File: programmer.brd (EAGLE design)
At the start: 35.3 x 22.1 mm, 20 parts, among them IC1 74ABT125DB, U1 ATMEGA8U2, X1 16MHz

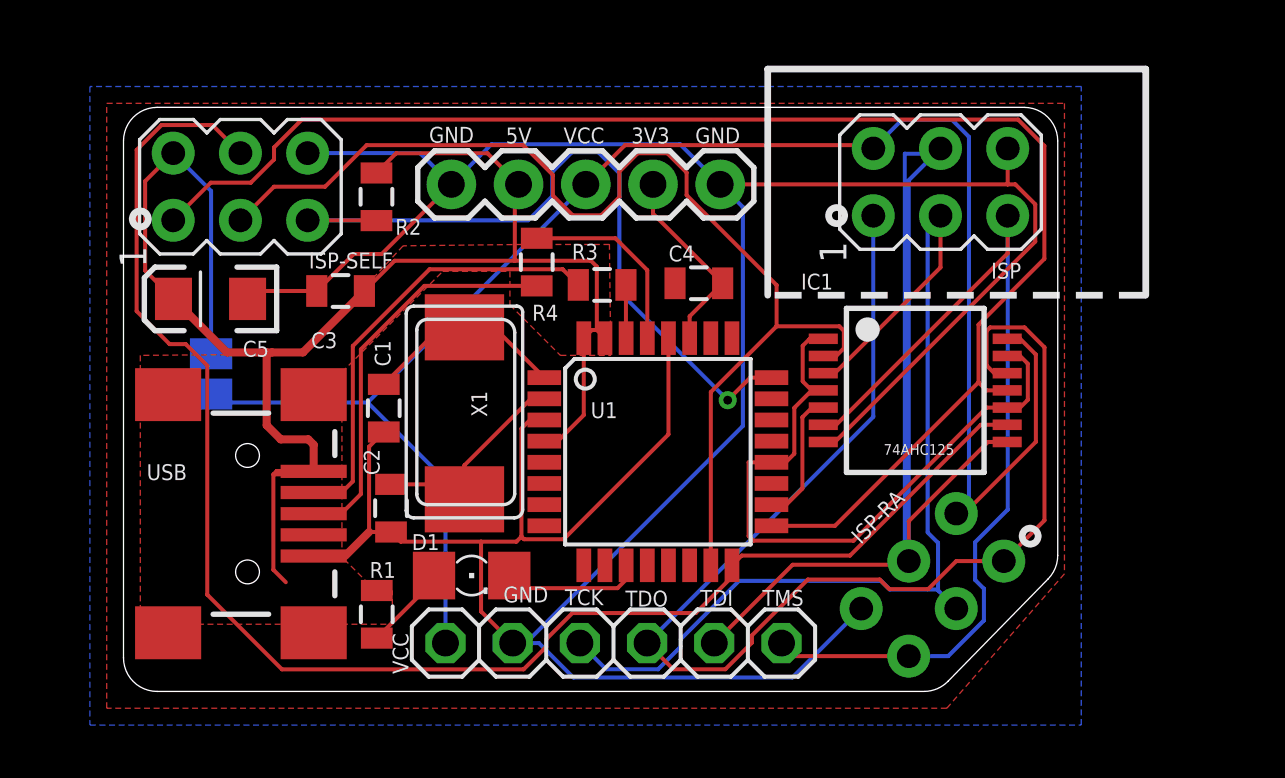
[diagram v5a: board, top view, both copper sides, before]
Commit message: Improved power and GND polygons, moved sowbug.com to a place where it won't get drilled
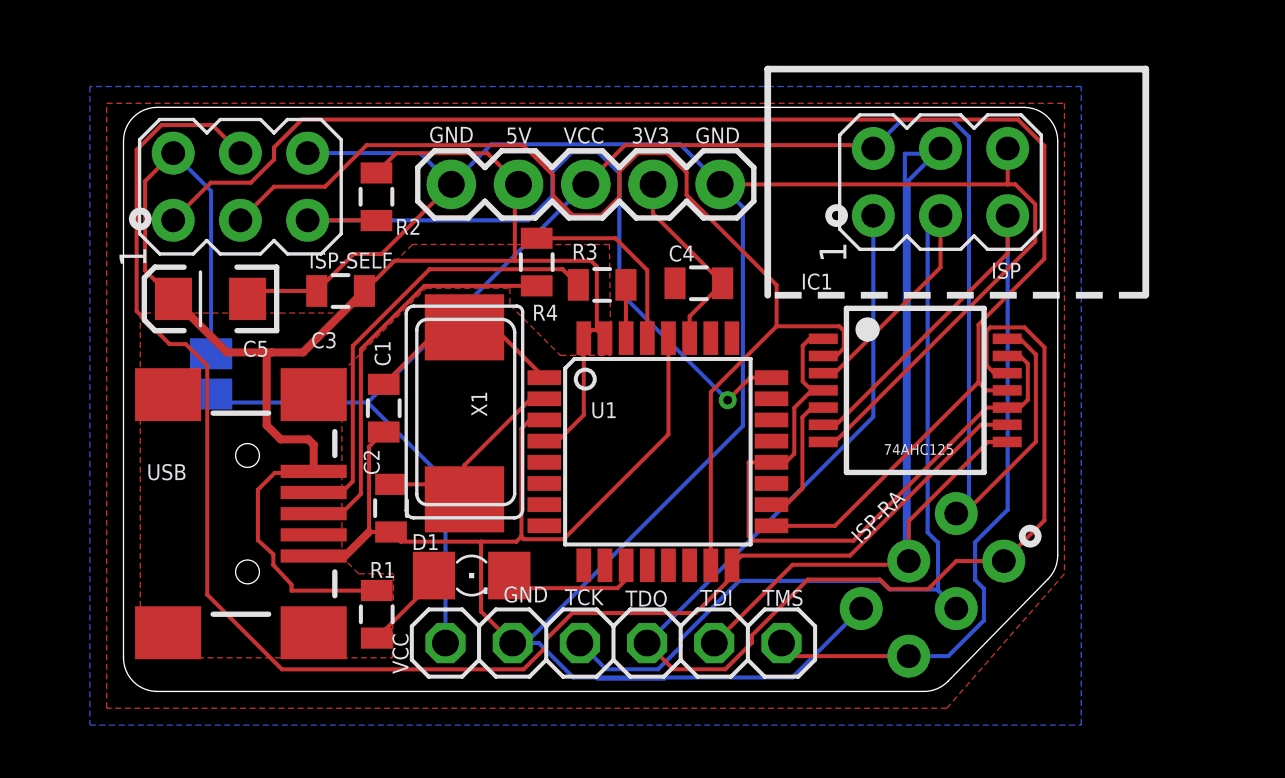
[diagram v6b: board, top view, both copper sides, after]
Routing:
- net 5V: track 64.1 -> 67.7 mm
- net N$1: track 0.00 -> 2.54 mm
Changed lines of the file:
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@@
 <layer number="19" name="Unrouted" color="6" fill="1" visible="yes" active="yes"/>
 <layer number="20" name="Dimension" color="15" fill="1" visible="yes" active="yes"/>
-<layer number="21" name="tPlace" color="7" fill="1" visible="yes" active="yes"/>
+<layer number="21" name="tPlace" color="7" fill="1" visible="no" active="yes"/>
 <layer number="22" name="bPlace" color="7" fill="1" visible="yes" active="yes"/>
-<layer number="23" name="tOrigins" color="15" fill="1" visible="yes" active="yes"/>
+<layer number="23" name="tOrigins" color="15" fill="1" visible="no" active="yes"/>
 <layer number="24" name="bOrigins" color="15" fill="1" visible="yes" active="yes"/>
-<layer number="25" name="tNames" color="7" fill="1" visible="yes" active="yes"/>
+<layer number="25" name="tNames" color="7" fill="1" visible="no" active="yes"/>
 <layer number="26" name="bNames" color="7" fill="1" visible="yes" active="yes"/>
 <layer number="27" name="tValues" color="7" fill="1" visible="yes" active="yes"/>
@@
 <layer number="37" name="tTest" color="7" fill="1" visible="no" active="yes"/>
 <layer number="38" name="bTest" color="7" fill="1" visible="no" active="yes"/>
-<layer number="39" name="tKeepout" color="4" fill="11" visible="yes" active="yes"/>
-<layer number="40" name="bKeepout" color="1" fill="11" visible="yes" active="yes"/>
-<layer number="41" name="tRestrict" color="4" fill="10" visible="yes" active="yes"/>
-<layer number="42" name="bRestrict" color="1" fill="10" visible="yes" active="yes"/>
-<layer number="43" name="vRestrict" color="2" fill="10" visible="yes" active="yes"/>
+<layer number="39" name="tKeepout" color="4" fill="11" visible="no" active="yes"/>
+<layer number="40" name="bKeepout" color="1" fill="11" visible="no" active="yes"/>
+<layer number="41" name="tRestrict" color="4" fill="10" visible="no" active="yes"/>
+<layer number="42" name="bRestrict" color="1" fill="10" visible="no" active="yes"/>
+<layer number="43" name="vRestrict" color="2" fill="10" visible="no" active="yes"/>
 <layer number="44" name="Drills" color="7" fill="1" visible="no" active="yes"/>
 <layer number="45" name="Holes" color="7" fill="1" visible="no" active="yes"/>
 <layer number="46" name="Milling" color="3" fill="1" visible="no" active="yes"/>
 <layer number="47" name="Measures" color="7" fill="1" visible="no" active="yes"/>
-<layer number="48" name="Document" color="7" fill="1" visible="yes" active="yes"/>
-<layer number="49" name="Reference" color="7" fill="1" visible="yes" active="yes"/>
+<layer number="48" name="Document" color="7" fill="1" visible="no" active="yes"/>
+<layer number="49" name="Reference" color="7" fill="1" visible="no" active="yes"/>
 <layer number="50" name="dxf" color="7" fill="1" visible="no" active="no"/>
-<layer number="51" name="tDocu" color="7" fill="1" visible="yes" active="yes"/>
+<layer number="51" name="tDocu" color="7" fill="1" visible="no" active="yes"/>
 <layer number="52" name="bDocu" color="7" fill="1" visible="yes" active="yes"/>
 <layer number="53" name="tGND_GNDA" color="7" fill="9" visible="no" active="no"/>
@@
 <layer number="109" name="fp9" color="7" fill="1" visible="no" active="yes"/>
 <layer number="110" name="fp0" color="7" fill="1" visible="no" active="yes"/>
-<layer number="111" name="LPC17xx" color="7" fill="1" visible="yes" active="yes"/>
-<layer number="112" name="tSilk" color="7" fill="1" visible="yes" active="yes"/>
+<layer number="111" name="LPC17xx" color="7" fill="1" visible="no" active="yes"/>
+<layer number="112" name="tSilk" color="7" fill="1" visible="no" active="yes"/>
 <layer number="116" name="Patch_BOT" color="9" fill="4" visible="no" active="yes"/>
 <layer number="121" name="_tsilk" color="7" fill="1" visible="no" active="yes"/>
@@
 <layer number="124" name="bTestmark" color="7" fill="1" visible="no" active="yes"/>
 <layer number="125" name="_tNames" color="7" fill="1" visible="no" active="yes"/>
-<layer number="126" name="_bNames" color="7" fill="1" visible="yes" active="yes"/>
-<layer number="127" name="_tValues" color="7" fill="1" visible="yes" active="yes"/>
-<layer number="128" name="_bValues" color="7" fill="1" visible="yes" active="yes"/>
+<layer number="126" name="_bNames" color="7" fill="1" visible="no" active="yes"/>
+<layer number="127" name="_tValues" color="7" fill="1" visible="no" active="yes"/>
+<layer number="128" name="_bValues" color="7" fill="1" visible="no" active="yes"/>
 <layer number="131" name="tAdjust" color="7" fill="1" visible="no" active="yes"/>
 <layer number="132" name="bAdjust" color="7" fill="1" visible="no" active="yes"/>
 <layer number="144" name="Drill_legend" color="7" fill="1" visible="no" active="yes"/>
 <layer number="151" name="HeatSink" color="7" fill="1" visible="no" active="yes"/>
-<layer number="152" name="_bDocu" color="7" fill="1" visible="yes" active="yes"/>
-<layer number="199" name="Contour" color="7" fill="1" visible="yes" active="yes"/>
+<layer number="152" name="_bDocu" color="7" fill="1" visible="no" active="yes"/>
+<layer number="199" name="Contour" color="7" fill="1" visible="no" active="yes"/>
 <layer number="200" name="200bmp" color="1" fill="10" visible="no" active="yes"/>
 <layer number="201" name="201bmp" color="2" fill="10" visible="no" active="yes"/>
@@
 <layer number="223" name="223bmp" color="24" fill="1" visible="no" active="no"/>
 <layer number="224" name="224bmp" color="25" fill="1" visible="no" active="no"/>
-<layer number="248" name="Housing" color="7" fill="1" visible="yes" active="yes"/>
-<layer number="249" name="Edge" color="7" fill="1" visible="yes" active="yes"/>
+<layer number="248" name="Housing" color="7" fill="1" visible="no" active="yes"/>
+<layer number="249" name="Edge" color="7" fill="1" visible="no" active="yes"/>
 <layer number="250" name="Descript" color="3" fill="1" visible="no" active="no"/>
 <layer number="251" name="SMDround" color="12" fill="11" visible="no" active="no"/>
@@
 <wire x1="34.036" y1="22.0726" x2="1.27" y2="22.0726" width="0" layer="20"/>
 <wire x1="1.27" y1="22.0726" x2="0" y2="20.8026" width="0" layer="20" curve="90"/>
-<text x="20.2692" y="16.0274" size="1.778" layer="22" font="vector" ratio="18" rot="MR0" align="bottom-center">sowbug.com</text>
+<text x="19.6342" y="15.3924" size="1.778" layer="22" font="vector" ratio="18" rot="MR0" align="bottom-center">sowbug.com</text>
 <text x="14.7574" y="8.9408" size="1.778" layer="22" font="vector" ratio="18" rot="MR0" align="bottom-right">MISO 1</text>
 <text x="13.4874" y="8.9408" size="1.778" layer="22" font="vector" ratio="18" rot="MR0">2 VCC</text>
@@
 <wire x1="5.3975" y1="12.7" x2="5.4102" y2="12.7" width="0.1524" layer="1"/>
 <wire x1="5.3975" y1="12.7" x2="5.3975" y2="12.8109" width="0.1524" layer="1"/>
-<wire x1="6.1341" y1="4.1275" x2="5.6642" y2="4.5974" width="0.1524" layer="1"/>
 <wire x1="6.8201" y1="8.3312" x2="7.1868" y2="8.3169" width="0.1524" layer="1"/>
-<wire x1="5.6642" y1="4.5974" x2="5.6642" y2="8.2042" width="0.1524" layer="1"/>
-<wire x1="6.8201" y1="8.3312" x2="5.7912" y2="8.3312" width="0.1524" layer="1"/>
-<wire x1="5.7912" y1="8.3312" x2="5.715" y2="8.255" width="0.1524" layer="1"/>
-<wire x1="5.6642" y1="8.2042" x2="7.0741" y2="8.2042" width="0.1524" layer="1"/>
 <wire x1="7.0741" y1="8.2042" x2="7.1868" y2="8.3169" width="0.1524" layer="1"/>
 <polygon width="0.1524" layer="1">
-<vertex x="0.635" y="12.7"/>
-<vertex x="0.635" y="2.54"/>
-<vertex x="10.16" y="2.54"/>
-<vertex x="10.16" y="3.81"/>
-<vertex x="9.525" y="3.81"/>
+<vertex x="0.635" y="14.3002"/>
+<vertex x="0.635" y="1.27"/>
+<vertex x="10.16" y="1.27"/>
+<vertex x="10.2108" y="4.445"/>
+<vertex x="8.89" y="4.445"/>
 <vertex x="8.255" y="5.08"/>
 <vertex x="8.255" y="12.065"/>
-<vertex x="12.065" y="15.875"/>
-<vertex x="14.605" y="15.875"/>
+<vertex x="11.43" y="15.24"/>
+<vertex x="14.605" y="15.24"/>
 <vertex x="14.605" y="14.605"/>
 <vertex x="16.51" y="12.7"/>
 <vertex x="18.415" y="12.7"/>
 <vertex x="18.3642" y="16.891"/>
-<vertex x="15.0622" y="16.891"/>
-<vertex x="10.5664" y="16.8402"/>
-<vertex x="6.7818" y="12.7508"/>
+<vertex x="10.922" y="16.891"/>
+<vertex x="8.3058" y="14.3002"/>
 </polygon>
+<wire x1="9.525" y1="4.1275" x2="9.2075" y2="3.81" width="0.1524" layer="1"/>
+<wire x1="7.1868" y1="8.3169" x2="7.1249" y2="8.255" width="0.1524" layer="1"/>
+<wire x1="7.1249" y1="8.255" x2="5.715" y2="8.255" width="0.1524" layer="1"/>
+<wire x1="5.715" y1="8.255" x2="5.08" y2="7.62" width="0.1524" layer="1"/>
+<wire x1="5.08" y1="7.62" x2="5.08" y2="5.715" width="0.1524" layer="1"/>
+<wire x1="5.08" y1="5.715" x2="5.6642" y2="5.1816" width="0.1524" layer="1"/>
+<wire x1="5.6642" y1="5.1816" x2="5.6642" y2="4.7752" width="0.1524" layer="1"/>
+<wire x1="5.6642" y1="4.7752" x2="6.35" y2="4.0386" width="0.1524" layer="1"/>
+<wire x1="6.35" y1="4.0386" x2="6.35" y2="3.81" width="0.1524" layer="1"/>
+<wire x1="6.35" y1="3.81" x2="9.5676" y2="3.81" width="0.1524" layer="1"/>
+<wire x1="9.5676" y1="3.81" x2="9.5714" y2="3.8138" width="0.1524" layer="1"/>
 </signal>
 <signal name="RST">
@@
 <wire x1="9.5485" y1="17.8043" x2="9.5594" y2="17.7934" width="0.1524" layer="1"/>
 </signal>
+<signal name="N$1">
+<wire x1="17.907" y1="0.4826" x2="20.447" y2="0.4826" width="0.1524" layer="16"/>
+</signal>
 </signals>
+<errors>
+</errors>
 </board>
 </drawing>

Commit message: Beefed up GND on bottom layer; cleaned up messy thermal/routing interaction near uC power
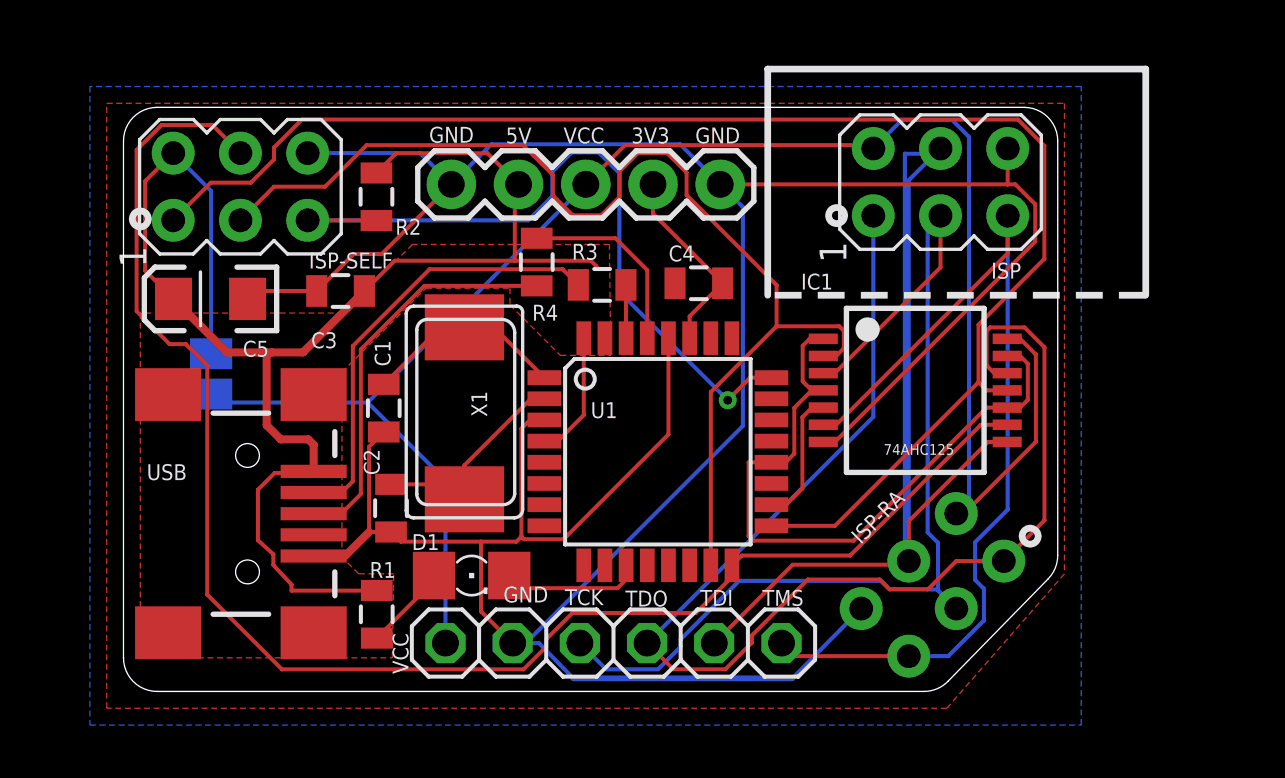
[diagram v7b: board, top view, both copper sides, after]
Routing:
- net 5V: track 67.7 -> 64.3 mm
- net N$1: track 2.54 -> 0.00 mm
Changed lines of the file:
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@@
 <wire x1="13.9079" y1="20.6801" x2="21.0325" y2="20.6801" width="0.1524" layer="16"/>
 <wire x1="21.0325" y1="20.6801" x2="22.5502" y2="19.1624" width="0.1524" layer="16"/>
-<wire x1="15.6981" y1="1.8281" x2="16.9995" y2="0.5267" width="0.1524" layer="16"/>
-<wire x1="16.9995" y1="0.5267" x2="25.2758" y2="0.5267" width="0.1524" layer="16"/>
-<wire x1="25.2758" y1="0.5267" x2="27.8798" y2="3.1307" width="0.1524" layer="16"/>
+<wire x1="15.6981" y1="1.8281" x2="16.9995" y2="0.49368125" width="0.1524" layer="16"/>
+<wire x1="16.9995" y1="0.49368125" x2="25.2758" y2="0.49368125" width="0.2159" layer="16"/>
+<wire x1="25.2758" y1="0.49368125" x2="27.8798" y2="3.1307" width="0.1524" layer="16"/>
 <wire x1="26.4459" y1="9.4269" x2="26.8839" y2="9.4269" width="0.1524" layer="1"/>
 <wire x1="26.8839" y1="9.4269" x2="34.457" y2="17" width="0.1524" layer="1"/>
@@
 <wire x1="17.3949" y1="10.4436" x2="16.4103" y2="9.459" width="0.1524" layer="1"/>
 <wire x1="16.4103" y1="9.459" x2="15.9023" y2="9.459" width="0.1524" layer="1"/>
-<wire x1="17.8875" y1="13.659" x2="17.7023" y2="13.659" width="0.1524" layer="1"/>
-<wire x1="17.7023" y1="13.659" x2="17.3949" y2="13.3516" width="0.1524" layer="1"/>
-<wire x1="17.8875" y1="13.659" x2="17.8875" y2="16.0546" width="0.1524" layer="1"/>
 <wire x1="17.8875" y1="16.0546" x2="17.6656" y2="16.2765" width="0.1524" layer="1"/>
 <wire x1="17.6656" y1="16.2765" x2="14.7881" y2="16.2765" width="0.1524" layer="1"/>
-<wire x1="18.1949" y1="13.3516" x2="17.8875" y2="13.659" width="0.1524" layer="1"/>
 <wire x1="14.9302" y1="19.1624" x2="14.7881" y2="19.0203" width="0.1524" layer="1"/>
 <wire x1="14.7881" y1="19.0203" x2="14.7881" y2="16.2765" width="0.1524" layer="1"/>
@@
 <wire x1="9.5485" y1="17.8043" x2="9.5594" y2="17.7934" width="0.1524" layer="1"/>
 </signal>
-<signal name="N$1">
-<wire x1="17.907" y1="0.4826" x2="20.447" y2="0.4826" width="0.1524" layer="16"/>
-</signal>
 </signals>
-<errors>
-</errors>
 </board>
 </drawing>
